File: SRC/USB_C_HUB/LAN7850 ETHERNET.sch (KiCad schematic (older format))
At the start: 41 parts

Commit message: ALL DONE BUT THE HDMI SECTION. NEED FOOTPRINT ASSIGNMENT
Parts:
- T1: renamed from T?; footprint H5008FNL -> SamacSys_Parts_2:H5008FNL
- gave numbers to parts that had none: 40

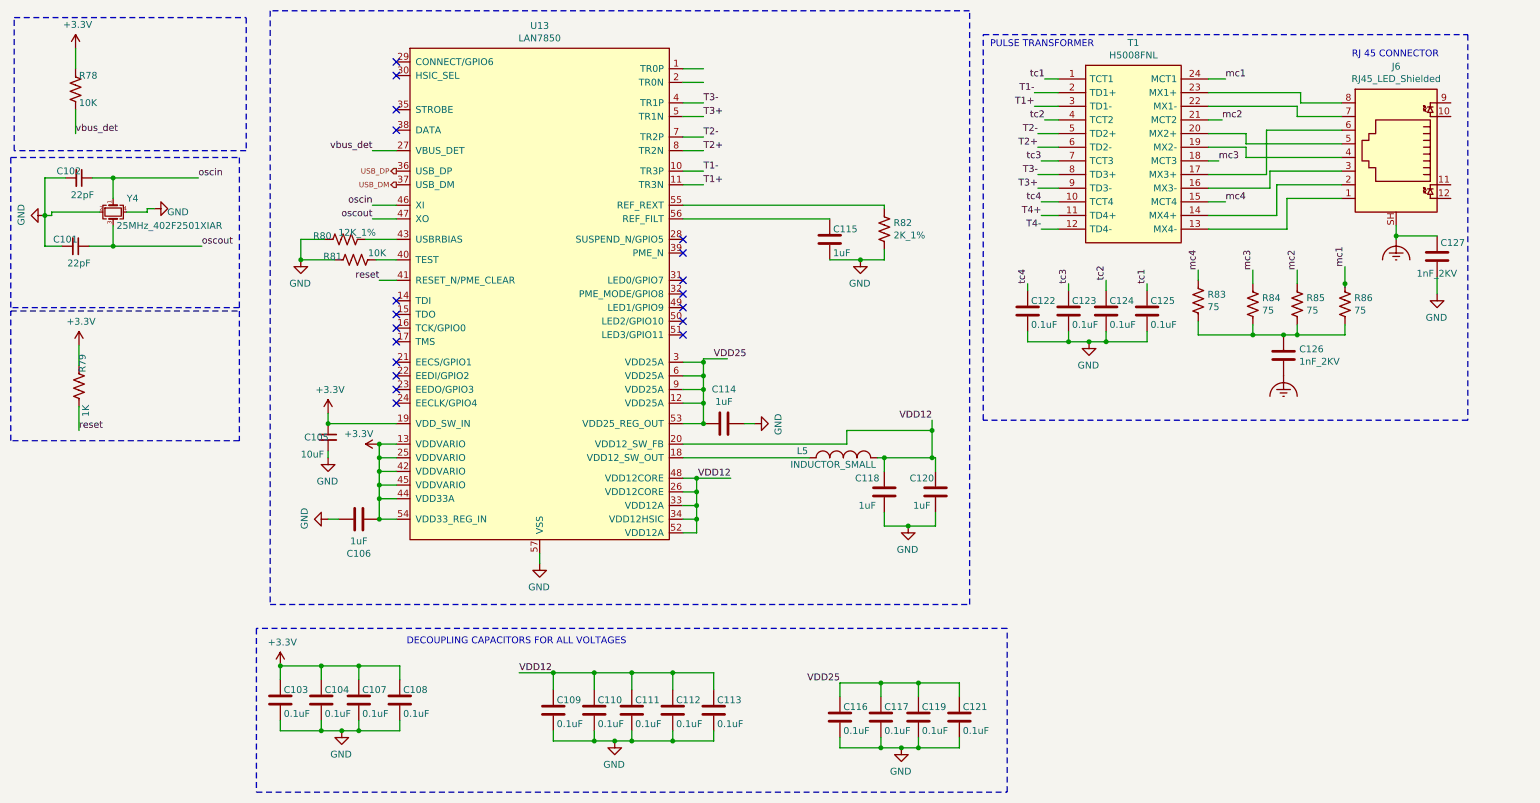
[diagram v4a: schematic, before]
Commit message: schematic capture complete. Pending Footprint assignment. accetable Errors=21
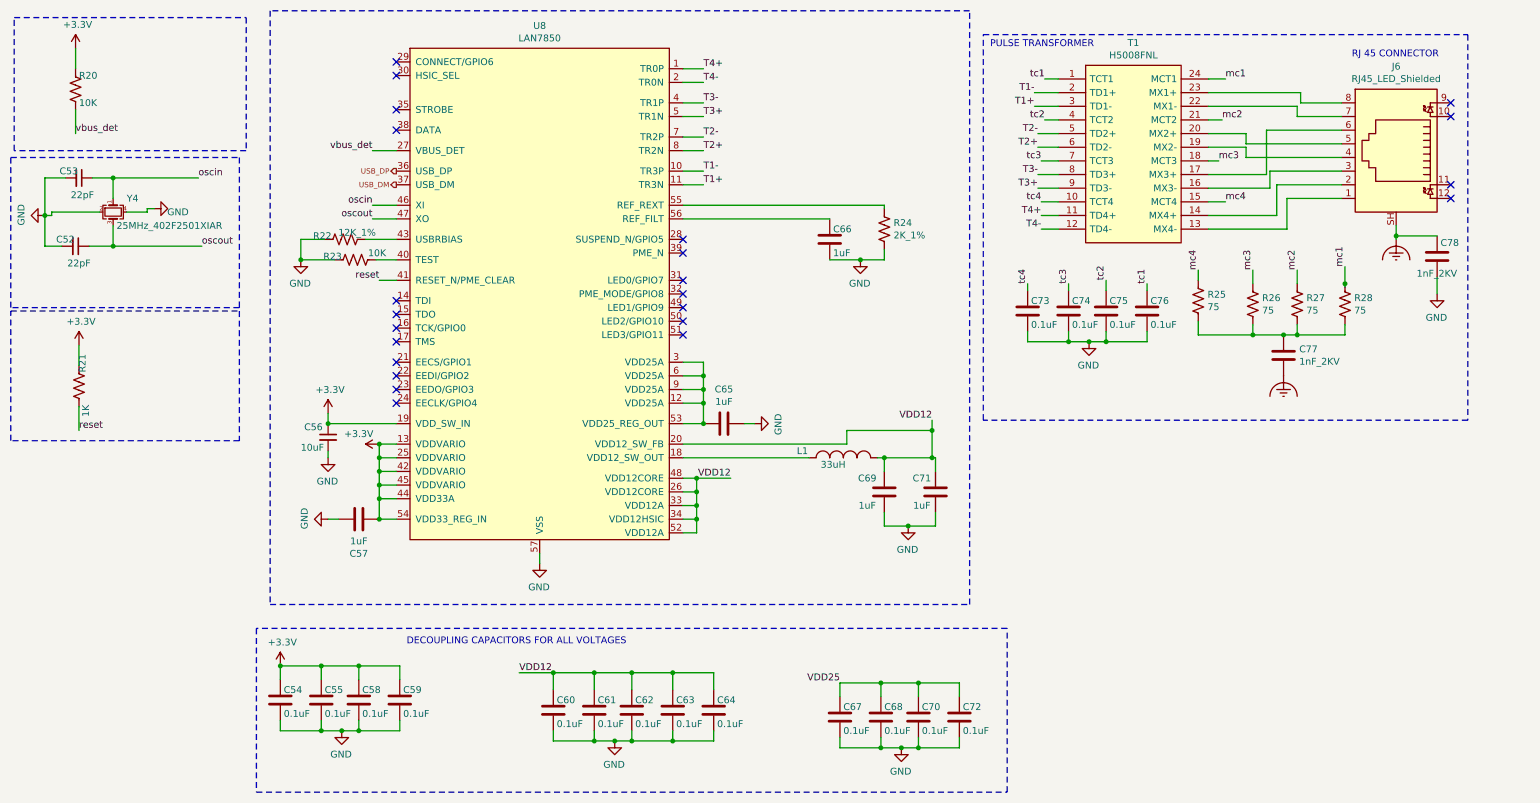
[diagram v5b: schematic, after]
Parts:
- L1: renamed from L5; value INDUCTOR_SMALL -> 33uH; Mfr No. (none) -> PA4332.332NLT
- renumbered C101 to C52, C102 to C53, C103 to C54, C104 to C55, C105 to C56, C106 to C57, C107 to C58, C108 to C59, C109 to C60, C110 to C61, C111 to C62, C112 to C63, C113 to C64, C114 to C65, C115 to C66, C116 to C67, C117 to C68, C118 to C69, C119 to C70, C120 to C71, C121 to C72, C122 to C73, C123 to C74, C124 to C75, C125 to C76, C126 to C77, C127 to C78, R78 to R20, R79 to R21, R80 to R22, R81 to R23, R82 to R24, R83 to R25, R84 to R26, R85 to R27, R86 to R28, U13 to U8
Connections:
- net T4+: now also U8.1 (TR0P)
- net T4-: now also U8.2 (TR0N)
- net VDD25: no longer C65.2, U8.12 (VDD25A), U8.3 (VDD25A), U8.53 (VDD25_REG_OUT), U8.6 (VDD25A), U8.9 (VDD25A)
- new net: C65.2, U8.12 (VDD25A), U8.3 (VDD25A), U8.53 (VDD25_REG_OUT), U8.6 (VDD25A), U8.9 (VDD25A)
- no-connect marks 19 -> 23

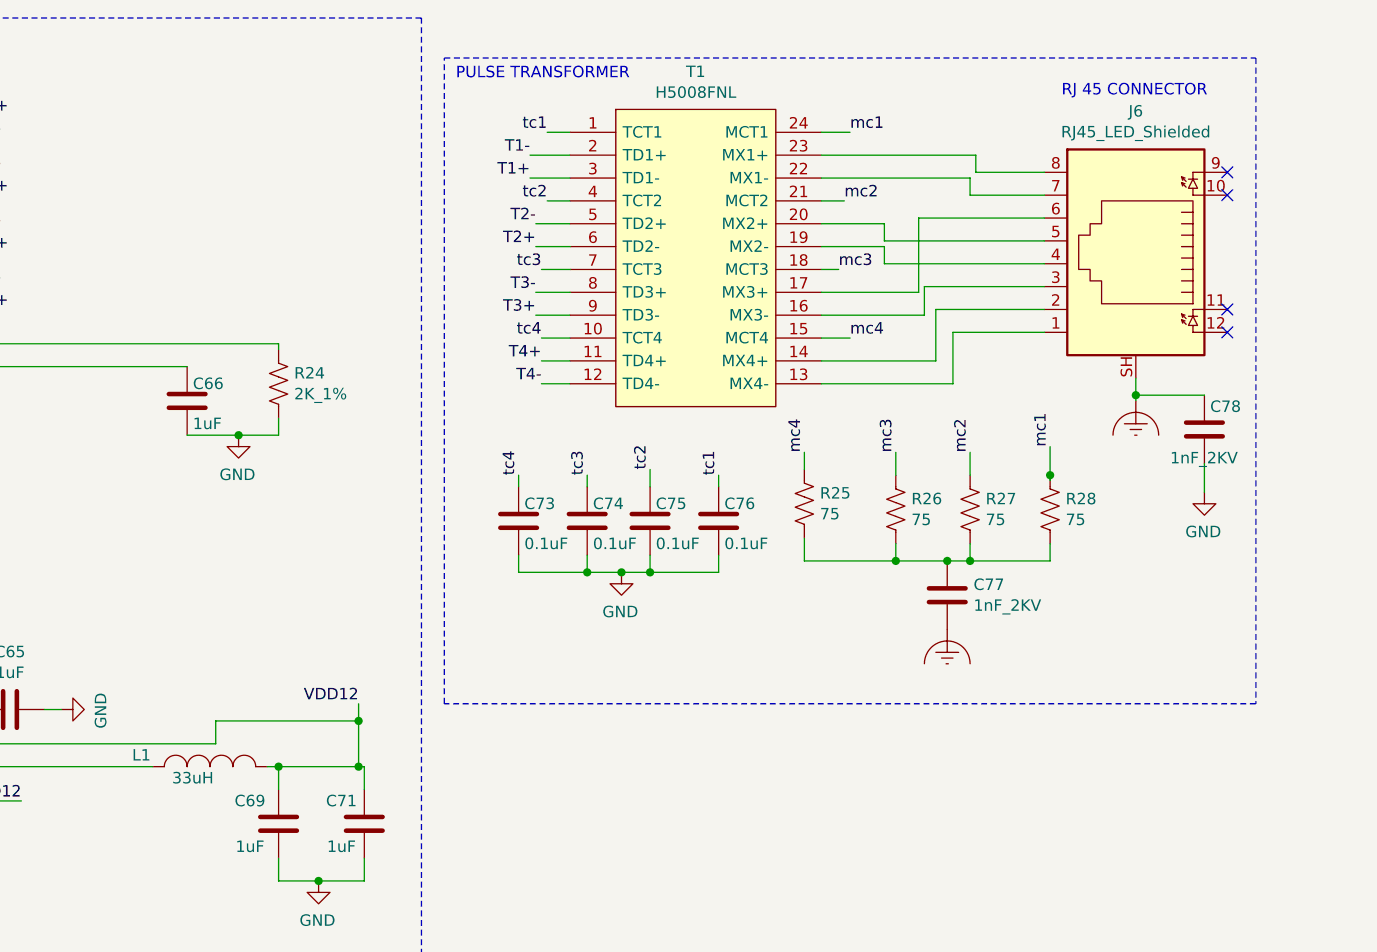
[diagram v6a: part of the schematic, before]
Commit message: schematic capture and footprint assignment complete. Pending approval
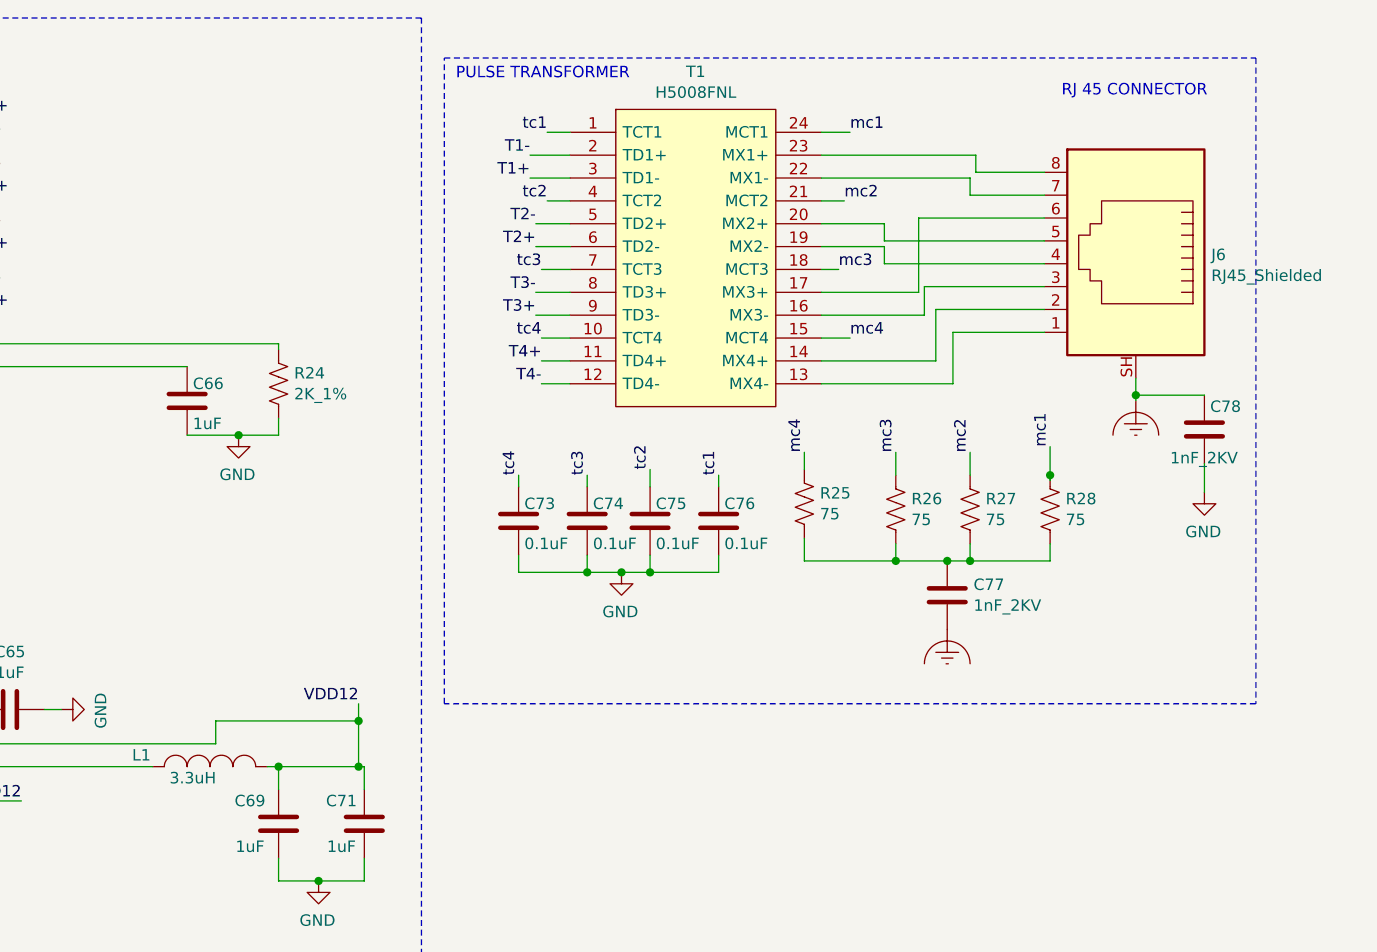
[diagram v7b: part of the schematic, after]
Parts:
- removed J6: RJ45_LED_Shielded, symbol Connector:RJ45_LED_Shielded
- added J6: RJ45_Shielded, footprints:CONN_RJ45-8Z, symbol Connector:RJ45_Shielded
- C52, C54, C55, C57, C58, C59, C60, C61, C62, C63, C64, C67, C68, C70, C72, C73, C74, C75, C76: footprint (none) -> Capacitor_SMD:C_0402_1005Metric
- C53: footprint (none) -> Capacitor_SMD:C_0402_1005Metric; Mfr No (none) -> CC0402JRNPO9BN220
- C56: footprint (none) -> Capacitor_SMD:C_0603_1608Metric
- C65: footprint (none) -> Capacitor_SMD:C_0402_1005Metric; Mfr No (none) -> CL05A105KQ5NNNC
- C66, C69, C71: footprint (none) -> Capacitor_SMD:C_0402_1005Metric; Mfr No. (none) -> CL05A105KQ5NNNC
- C77, C78: footprint (none) -> Capacitor_SMD:C_1206_3216Metric; Mfr No. (none) -> 1206B102K202NT
- L1: value 33uH -> 3.3uH; footprint (none) -> SamacSys_Parts_2:INDPM4040X200N; Mfr No. PA4332.332NLT -> 74405042033
- R20: footprint (none) -> Resistor_SMD:R_0402_1005Metric; Mfr No. (none) -> 0402WGF1002TCE
- R21, R23, R26, R27, R28: footprint (none) -> Resistor_SMD:R_0402_1005Metric
- R22: footprint (none) -> Resistor_SMD:R_0402_1005Metric; Mfr No (none) -> RTT021202FTH
- R24: footprint (none) -> Resistor_SMD:R_0402_1005Metric; Mfr No. (none) -> AC0402FR-072KL
- R25: footprint (none) -> Resistor_SMD:R_0402_1005Metric; Mfr No. (none) -> ERJPA2J750X
- U8: footprint (none) -> footprints:QFN40P700X700X100-57N
- Y4: footprint (none) -> Crystal:Crystal_SMD_2016-4Pin_2.0x1.6mm
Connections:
- net Earth_Clean: now also J6.SH
- net at T1.13 (MX4-): now also J6.1
- net at T1.14 (MX4+): now also J6.2
- net at T1.16 (MX3-): now also J6.3
- net at T1.19 (MX2-): now also J6.4
- net at T1.20 (MX2+): now also J6.5
- net at T1.17 (MX3+): now also J6.6
- net at T1.22 (MX1-): now also J6.7
- net at T1.23 (MX1+): now also J6.8
- no-connect marks 23 -> 19
